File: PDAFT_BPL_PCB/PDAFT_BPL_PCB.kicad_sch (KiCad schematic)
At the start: 15 parts

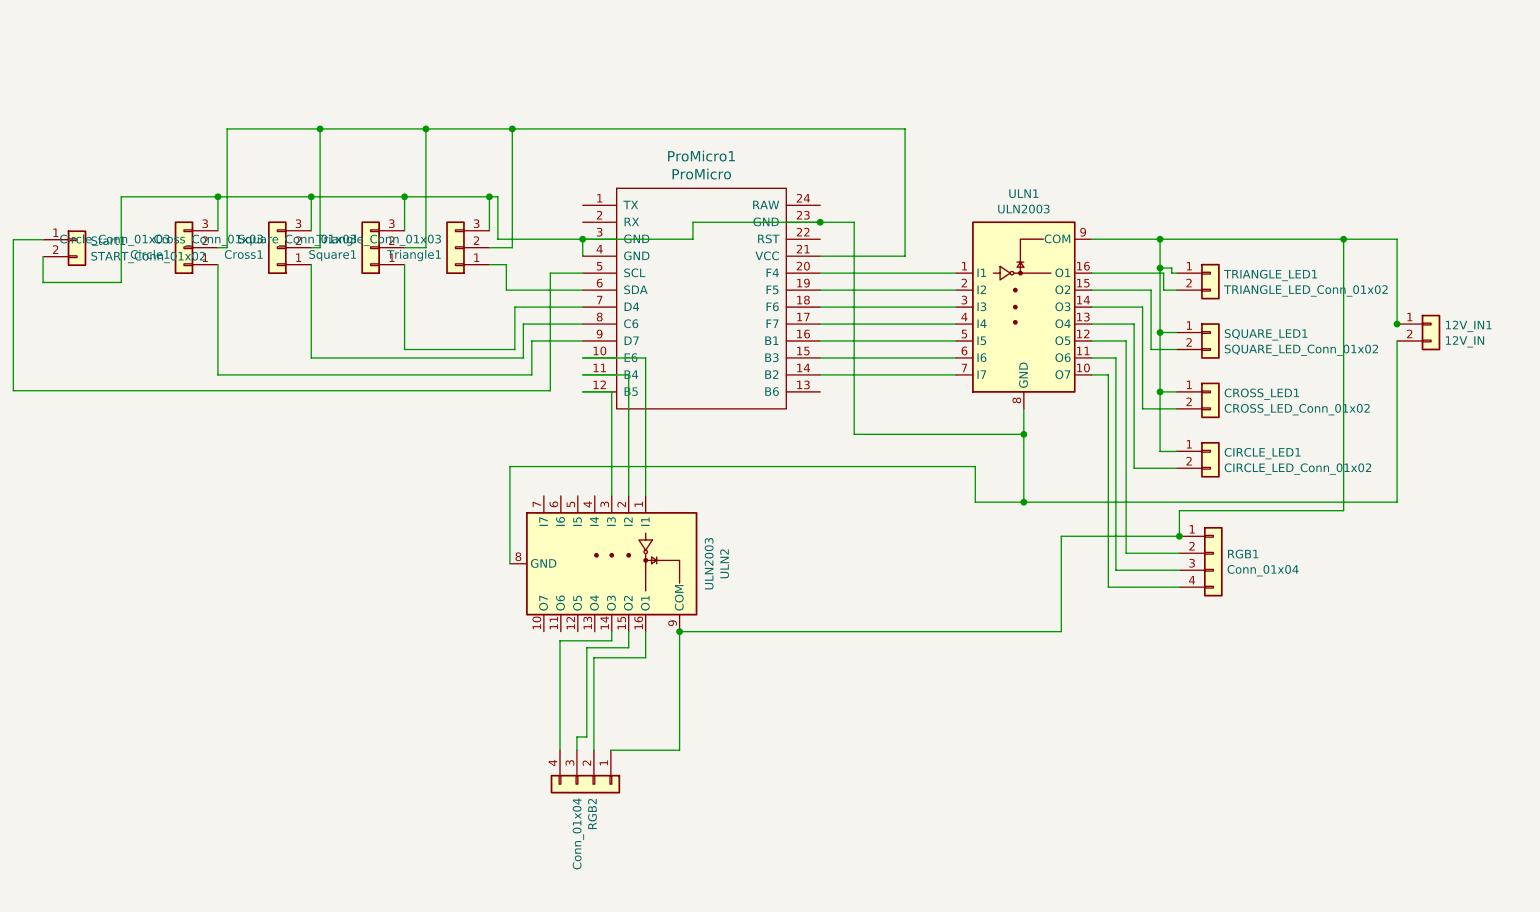
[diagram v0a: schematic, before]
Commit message: Update PCB
Update PCB to make fast write to registers in interruptions when received LEDs data by UART
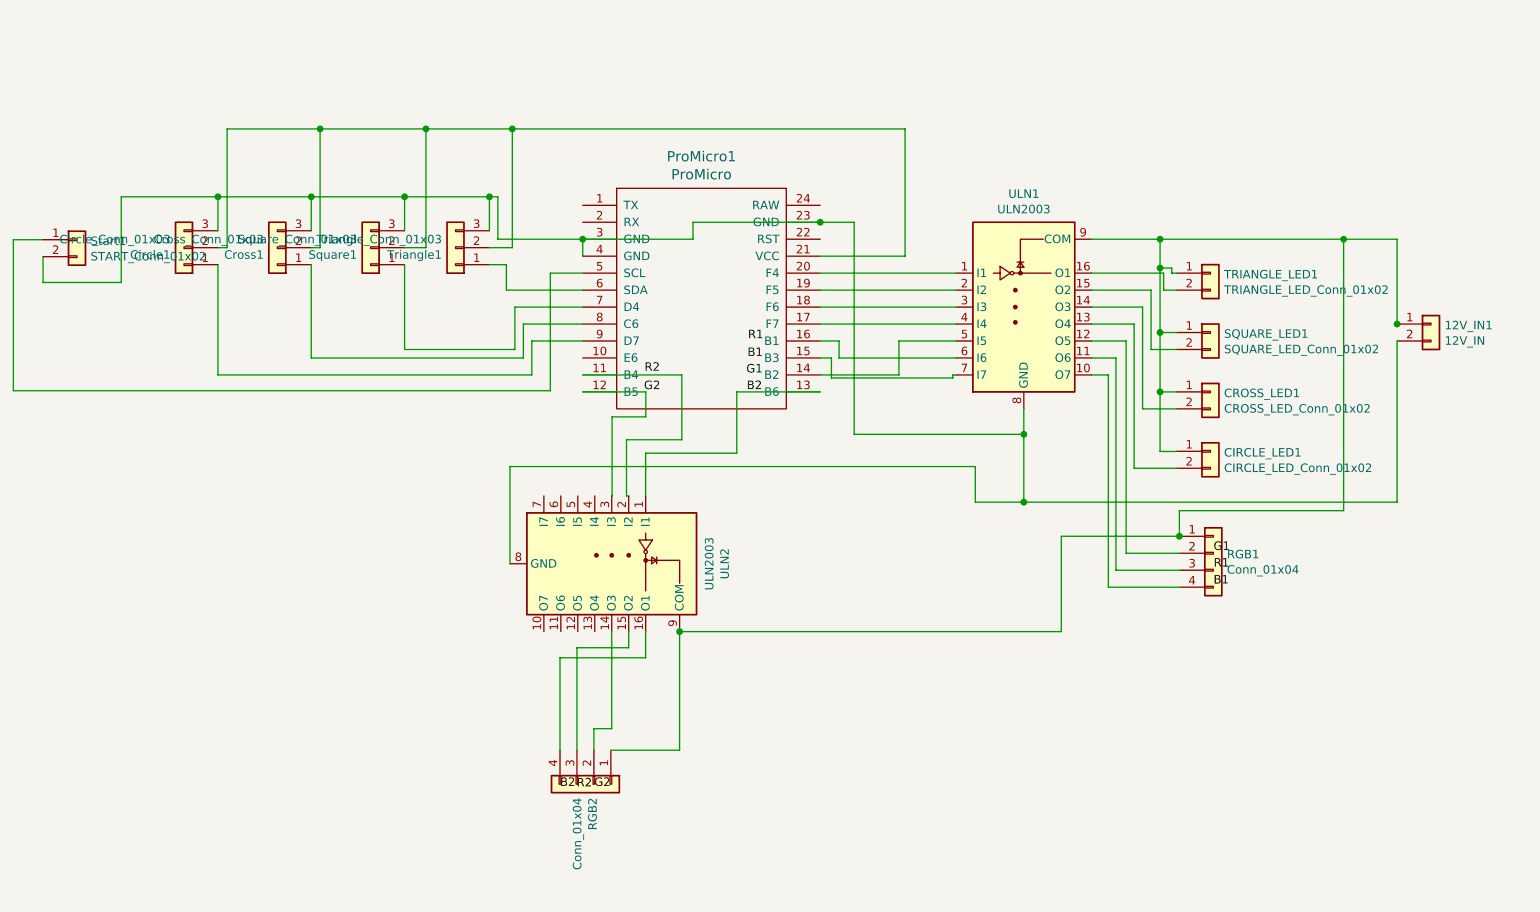
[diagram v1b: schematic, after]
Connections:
- net at ProMicro1.10 (E6): no longer ULN2.1 (I1)
- net at ProMicro1.13 (B6): now also ULN2.1 (I1)
- net at ProMicro1.14 (B2): now also ULN1.5 (I5); no longer ULN1.7 (I7)
- net at ProMicro1.15 (B3): now also ULN1.7 (I7); no longer ULN1.6 (I6)
- net at ProMicro1.16 (B1): now also ULN1.6 (I6); no longer ULN1.5 (I5)
- net at RGB2.2 (Pin_2): now also ULN2.14 (O3); no longer ULN2.16 (O1)
- net at RGB2.4 (Pin_4): now also ULN2.16 (O1); no longer ULN2.14 (O3)

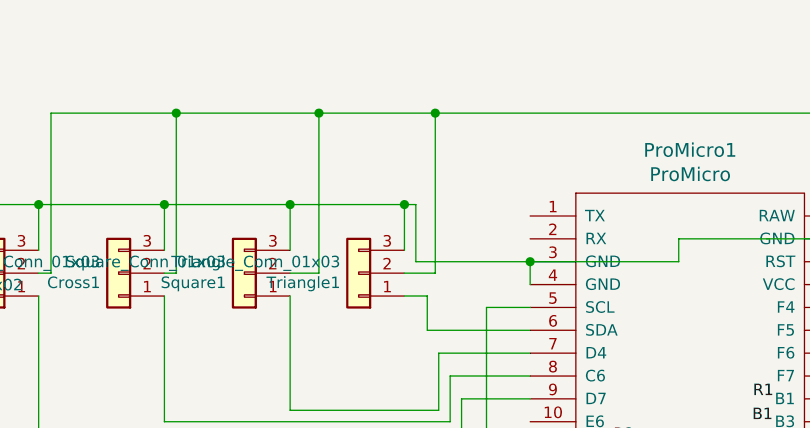
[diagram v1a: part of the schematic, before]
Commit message: Update of PCB and firmware
Updated PCB to have possibility to connect USB-TTL converter to use interuption in serial connection (program for it will be soon completed with various variants of use, now only SerialEvent1() interuption)
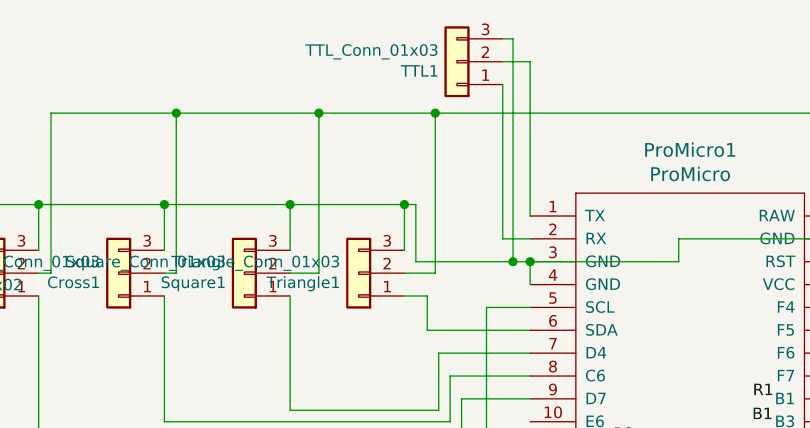
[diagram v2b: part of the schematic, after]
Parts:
- added TTL1: TTL_Conn_01x03, Connector_JST:JST_XH_B3B-XH-A_1x03_P2.50mm_Vertical, symbol Connector_Generic:Conn_01x03
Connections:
- net at ProMicro1.1 (TX): now also TTL1.2 (Pin_2)
- net at ProMicro1.2 (RX): now also TTL1.1 (Pin_1)
- net at 12V_IN1.2 (Pin_2), Circle1.3 (Pin_3), Cross1.3 (Pin_3)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: now also TTL1.3 (Pin_3)
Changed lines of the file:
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@@
   (junction (at 114.3 34.29) (diameter 1.016) (color 0 0 0 0))
   (junction (at 117.729 24.13) (diameter 1.016) (color 0 0 0 0))
+  (junction (at 126.365 40.64) (diameter 1.016) (color 0 0 0 0))
   (junction (at 128.27 40.64) (diameter 1.016) (color 0 0 0 0))
   (junction (at 142.7734 99.3902) (diameter 1.016) (color 0 0 0 0))
@@
     (stroke (width 0) (type solid) (color 0 0 0 0))
   )
-  (wire (pts (xy 115.57 40.64) (xy 128.27 40.64))
+  (wire (pts (xy 115.57 40.64) (xy 126.365 40.64))
     (stroke (width 0) (type solid) (color 0 0 0 0))
   )
@@
     (stroke (width 0) (type solid) (color 0 0 0 0))
   )
+  (wire (pts (xy 125.222 20.955) (xy 125.222 38.1))
+    (stroke (width 0) (type solid) (color 0 0 0 0))
+  )
+  (wire (pts (xy 125.222 38.1) (xy 128.27 38.1))
+    (stroke (width 0) (type solid) (color 0 0 0 0))
+  )
+  (wire (pts (xy 126.365 15.875) (xy 125.222 15.875))
+    (stroke (width 0) (type solid) (color 0 0 0 0))
+  )
+  (wire (pts (xy 126.365 40.64) (xy 126.365 15.875))
+    (stroke (width 0) (type solid) (color 0 0 0 0))
+  )
+  (wire (pts (xy 126.365 40.64) (xy 128.27 40.64))
+    (stroke (width 0) (type solid) (color 0 0 0 0))
+  )
   (wire (pts (xy 127.4064 101.8032) (xy 127.4064 117.1448))
     (stroke (width 0) (type solid) (color 0 0 0 0))
@@
     (stroke (width 0) (type solid) (color 0 0 0 0))
   )
+  (wire (pts (xy 128.27 18.415) (xy 125.222 18.415))
+    (stroke (width 0) (type solid) (color 0 0 0 0))
+  )
+  (wire (pts (xy 128.27 35.56) (xy 128.27 18.415))
+    (stroke (width 0) (type solid) (color 0 0 0 0))
+  )
   (wire (pts (xy 128.27 40.64) (xy 128.27 43.18))
     (stroke (width 0) (type solid) (color 0 0 0 0))
@@
     )
     (property "Datasheet" "~" (id 3) (at 109.22 41.91 0)
+      (effects (font (size 1.27 1.27)) hide)
+    )
+    (pin "1")
+    (pin "2")
+    (pin "3")
+  )
+  (symbol (lib_id "Connector_Generic:Conn_01x03") (at 120.142 18.415 180) (unit 1)
+    (in_bom yes) (on_board yes)
+    (property "Reference" "TTL1" (id 0) (at 118.11 19.482 0)
+      (effects (font (size 1.27 1.27)) (justify left))
+    )
+    (property "Value" "TTL_Conn_01x03" (id 1) (at 118.11 17.1704 0)
+      (effects (font (size 1.27 1.27)) (justify left))
+    )
+    (property "Footprint" "Connector_JST:JST_XH_B3B-XH-A_1x03_P2.50mm_Vertical" (id 2) (at 120.142 18.415 0)
+      (effects (font (size 1.27 1.27)) hide)
+    )
+    (property "Datasheet" "~" (id 3) (at 120.142 18.415 0)
       (effects (font (size 1.27 1.27)) hide)
     )
@@
       (reference "TRIANGLE_LED1") (unit 1) (value "TRIANGLE_LED_Conn_01x02") (footprint "Connector_JST:JST_XH_B2B-XH-A_1x02_P2.50mm_Vertical")
     )
+    (path "/6c9ab6ec-78e2-4203-b1a0-a08a20d9ebf7"
+      (reference "TTL1") (unit 1) (value "TTL_Conn_01x03") (footprint "Connector_JST:JST_XH_B3B-XH-A_1x03_P2.50mm_Vertical")
+    )
     (path "/00000000-0000-0000-0000-00005dc6a9fa"

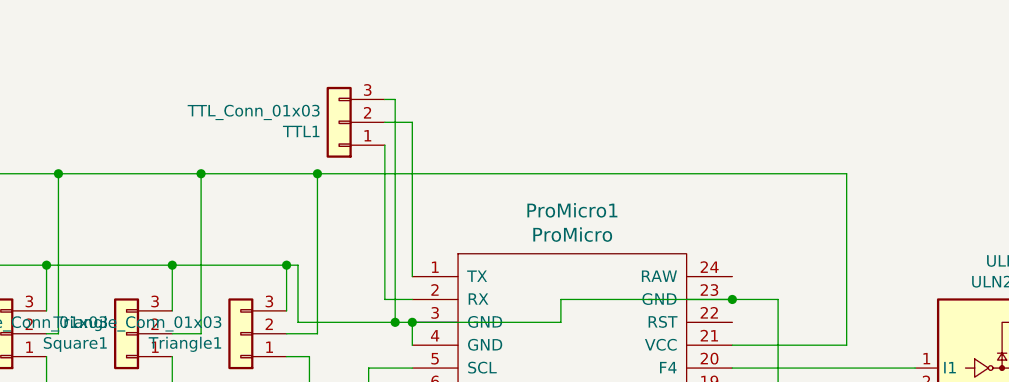
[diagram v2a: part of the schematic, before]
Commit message: Added +5v from TTL to use if needed
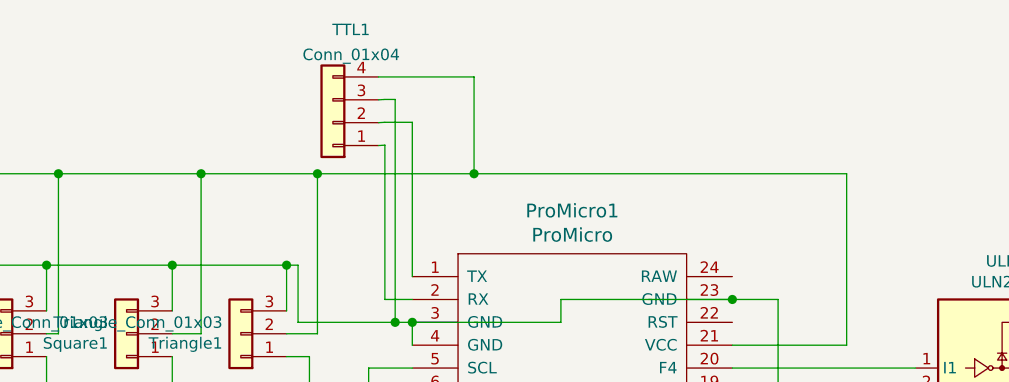
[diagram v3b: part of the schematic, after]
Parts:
- removed TTL1: TTL_Conn_01x03, Connector_JST:JST_XH_B3B-XH-A_1x03_P2.50mm_Vertical, symbol Connector_Generic:Conn_01x03
- added TTL1: Conn_01x04, Connector_JST:JST_XH_B4B-XH-A_1x04_P2.50mm_Vertical, symbol Connector_Generic:Conn_01x04
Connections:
- net at ProMicro1.1 (TX): now also TTL1.2 (Pin_2)
- net at ProMicro1.2 (RX): now also TTL1.1 (Pin_1)
- net at Circle1.2 (Pin_2), Cross1.2 (Pin_2), ProMicro1.21 (VCC)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: now also TTL1.4 (Pin_4)
- net at 12V_IN1.2 (Pin_2), Circle1.3 (Pin_3), Cross1.3 (Pin_3)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: now also TTL1.3 (Pin_3)
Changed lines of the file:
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@@
   (junction (at 126.365 40.64) (diameter 1.016) (color 0 0 0 0))
   (junction (at 128.27 40.64) (diameter 1.016) (color 0 0 0 0))
+  (junction (at 135.1314 24.13) (diameter 1.016) (color 0 0 0 0))
   (junction (at 142.7734 99.3902) (diameter 1.016) (color 0 0 0 0))
   (junction (at 163.83 38.1) (diameter 1.016) (color 0 0 0 0))
@@
     (stroke (width 0) (type solid) (color 0 0 0 0))
   )
-  (wire (pts (xy 117.729 24.13) (xy 176.53 24.13))
+  (wire (pts (xy 117.729 24.13) (xy 135.1314 24.13))
     (stroke (width 0) (type solid) (color 0 0 0 0))
   )
@@
     (stroke (width 0) (type solid) (color 0 0 0 0))
   )
+  (wire (pts (xy 124.5288 13.3761) (xy 135.1314 13.3761))
+    (stroke (width 0) (type solid) (color 0 0 0 0))
+  )
   (wire (pts (xy 124.8664 103.3018) (xy 137.6934 103.3018))
     (stroke (width 0) (type solid) (color 0 0 0 0))
@@
     (stroke (width 0) (type solid) (color 0 0 0 0))
   )
+  (wire (pts (xy 125.222 15.875) (xy 124.5288 15.9161))
+    (stroke (width 0) (type solid) (color 0 0 0 0))
+  )
+  (wire (pts (xy 125.222 18.415) (xy 124.5288 18.4561))
+    (stroke (width 0) (type solid) (color 0 0 0 0))
+  )
+  (wire (pts (xy 125.222 20.955) (xy 124.5288 20.9961))
+    (stroke (width 0) (type solid) (color 0 0 0 0))
+  )
   (wire (pts (xy 125.222 20.955) (xy 125.222 38.1))
     (stroke (width 0) (type solid) (color 0 0 0 0))
@@
     (stroke (width 0) (type solid) (color 0 0 0 0))
   )
+  (wire (pts (xy 135.1314 13.3761) (xy 135.1314 24.13))
+    (stroke (width 0) (type solid) (color 0 0 0 0))
+  )
+  (wire (pts (xy 135.1314 24.13) (xy 176.53 24.13))
+    (stroke (width 0) (type solid) (color 0 0 0 0))
+  )
   (wire (pts (xy 135.1534 99.3902) (xy 135.1534 101.8032))
     (stroke (width 0) (type solid) (color 0 0 0 0))
@@
     (pin "3")
   )
-  (symbol (lib_id "Connector_Generic:Conn_01x03") (at 120.142 18.415 180) (unit 1)
-    (in_bom yes) (on_board yes)
-    (property "Reference" "TTL1" (id 0) (at 118.11 19.482 0)
-      (effects (font (size 1.27 1.27)) (justify left))
-    )
-    (property "Value" "TTL_Conn_01x03" (id 1) (at 118.11 17.1704 0)
-      (effects (font (size 1.27 1.27)) (justify left))
-    )
-    (property "Footprint" "Connector_JST:JST_XH_B3B-XH-A_1x03_P2.50mm_Vertical" (id 2) (at 120.142 18.415 0)
-      (effects (font (size 1.27 1.27)) hide)
-    )
-    (property "Datasheet" "~" (id 3) (at 120.142 18.415 0)
-      (effects (font (size 1.27 1.27)) hide)
-    )
-    (pin "1")
-    (pin "2")
-    (pin "3")
+  (symbol (lib_id "Connector_Generic:Conn_01x04") (at 119.4488 18.4561 180) (unit 1)
+    (in_bom yes) (on_board yes) (fields_autoplaced)
+    (property "Reference" "TTL1" (id 0) (at 121.4808 8.1395 0))
+    (property "Value" "Conn_01x04" (id 1) (at 121.4808 10.9146 0))
+    (property "Footprint" "Connector_JST:JST_XH_B4B-XH-A_1x04_P2.50mm_Vertical" (id 2) (at 119.4488 18.4561 0)
+      (effects (font (size 1.27 1.27)) hide)
+    )
+    (property "Datasheet" "~" (id 3) (at 119.4488 18.4561 0)
+      (effects (font (size 1.27 1.27)) hide)
+    )
+    (pin "1")
+    (pin "2")
+    (pin "3")
+    (pin "4")
   )
   (symbol (lib_id "Connector_Generic:Conn_01x04") (at 129.9464 122.2248 270) (unit 1)
@@
       (reference "TRIANGLE_LED1") (unit 1) (value "TRIANGLE_LED_Conn_01x02") (footprint "Connector_JST:JST_XH_B2B-XH-A_1x02_P2.50mm_Vertical")
     )
-    (path "/6c9ab6ec-78e2-4203-b1a0-a08a20d9ebf7"
-      (reference "TTL1") (unit 1) (value "TTL_Conn_01x03") (footprint "Connector_JST:JST_XH_B3B-XH-A_1x03_P2.50mm_Vertical")
+    (path "/510bc63c-2fe1-4891-8ccf-9a5fbca68f62"
+      (reference "TTL1") (unit 1) (value "Conn_01x04") (footprint "Connector_JST:JST_XH_B4B-XH-A_1x04_P2.50mm_Vertical")
     )
     (path "/00000000-0000-0000-0000-00005dc6a9fa"
